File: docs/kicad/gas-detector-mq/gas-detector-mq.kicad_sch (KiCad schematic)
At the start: 8 parts, among them U1 ESP32_DevKit_V1, U2 MH-MQ-Sensor

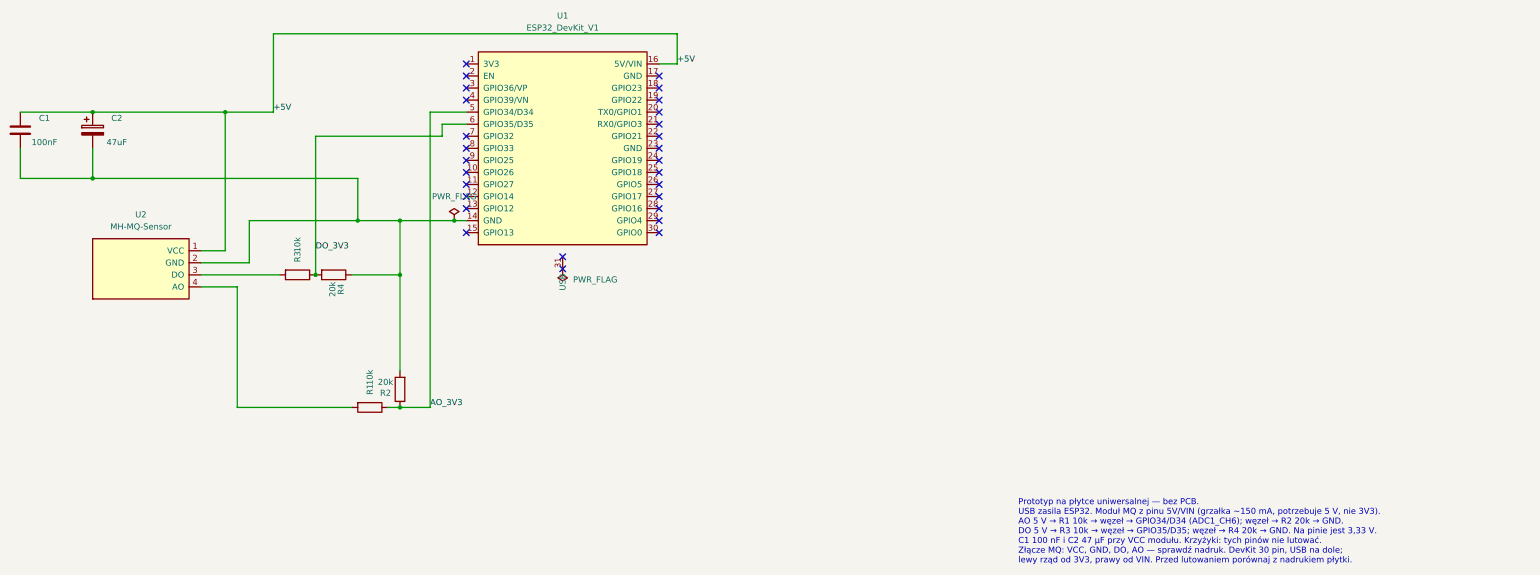
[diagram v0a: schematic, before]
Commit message: Zamień bulk 47 µF na 10 µF / 50 V.
Kondensator 100 nF zostaje. 1000 µF / 6,3 V nie wchodzi na szynę 5 V z USB: za mały zapas napięcia i duży udar przy wpięciu kabla.

Co-authored-by: michal.kalkowski <michal.kalkowski@sumup.com>
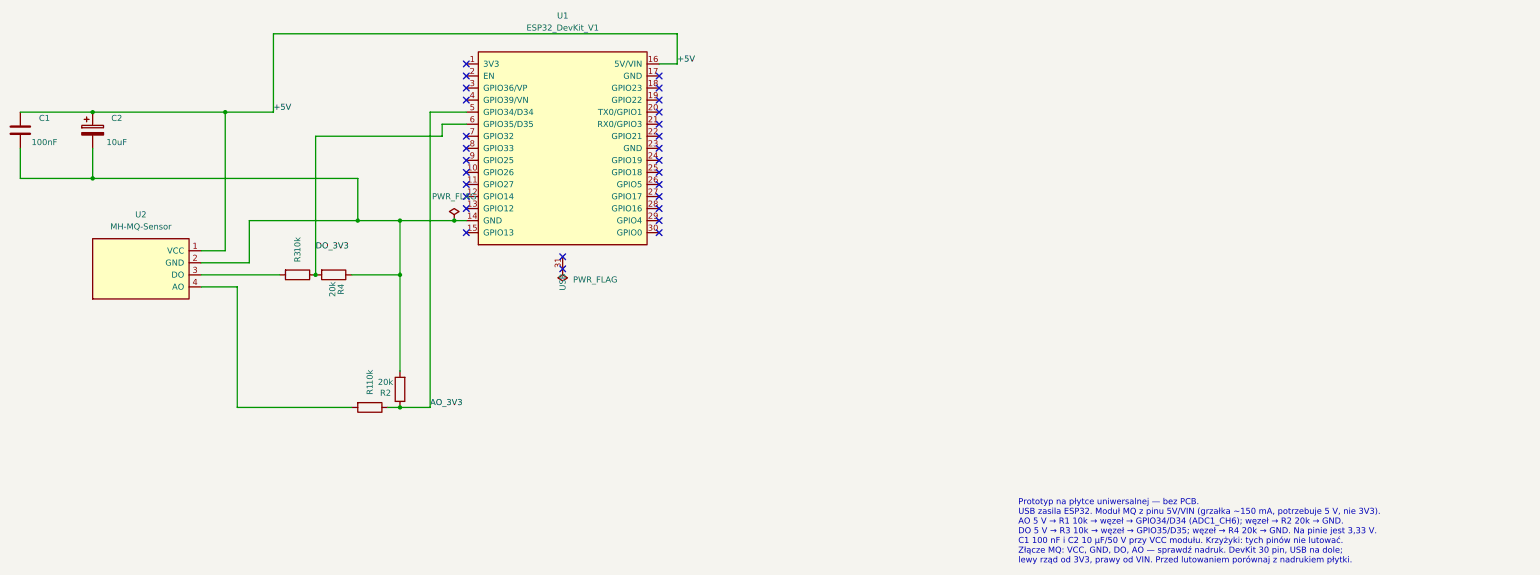
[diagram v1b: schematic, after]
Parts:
- C2: value 47uF -> 10uF
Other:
- note added: "Prototyp na płytce uniwersalnej — bez PCB. USB zasila ESP32. Moduł MQ z pinu 5V/VIN (grzałka ~150 mA, potrzebuje 5 V, nie 3V3). AO 5 V → R1 10k → węzeł → GPIO34/D34 (ADC1_CH6); węzeł → R2 20k → GND. DO 5 V → R3 10k → węzeł → GPIO35/D35; węzeł → R4 20k → GND. Na pinie jest 3,33 V. C1 100 nF i C2 10 µF/50 V przy VCC modułu. Krzyżyki: tych pinów nie lutować. Złącze MQ: VCC, GND, DO, AO — sprawdź nad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"
- note removed: "Prototyp na płytce uniwersalnej — bez PCB. USB zasila ESP32. Moduł MQ z pinu 5V/VIN (grzałka ~150 mA, potrzebuje 5 V, nie 3V3). AO 5 V → R1 10k → węzeł → GPIO34/D34 (ADC1_CH6); węzeł → R2 20k → GND. DO 5 V → R3 10k → węzeł → GPIO35/D35; węzeł → R4 20k → GND. Na pinie jest 3,33 V. C1 100 nF i C2 47 µF przy VCC modułu. Krzyżyki: tych pinów nie lutować. Złącze MQ: VCC, GND, DO, AO — sprawdź nadruk. 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"
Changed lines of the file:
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@@
 		(comment 3 "Założenie: DOIT DevKit V1 30 pin, USB na dole; złącze MQ VCC GND DO AO.")
 	)
-	(text "Prototyp na płytce uniwersalnej — bez PCB.\nUSB zasila ESP32. Moduł MQ z pinu 5V/VIN (grzałka ~150 mA, potrzebuje 5 V, nie 3V3).\nAO 5 V → R1 10k → węzeł → GPIO34/D34 (ADC1_CH6); węzeł → R2 20k → GND.\nDO 5 V → R3 10k → węzeł → GPIO35/D35; węzeł → R4 20k → GND. Na pinie jest 3,33 V.\nC1 100 nF i C2 47 µF przy VCC modułu. Krzyżyki: tych pinów nie lutować.\nZłącze MQ: VCC, GND, DO, AO — sprawdź nadruk. DevKit 30 pin, USB na dole;\nlewy rząd od 3V3, prawy od VIN. Przed lutowaniem porównaj z nadrukiem płytki."
+	(text "Prototyp na płytce uniwersalnej — bez PCB.\nUSB zasila ESP32. Moduł MQ z pinu 5V/VIN (grzałka ~150 mA, potrzebuje 5 V, nie 3V3).\nAO 5 V → R1 10k → węzeł → GPIO34/D34 (ADC1_CH6); węzeł → R2 20k → GND.\nDO 5 V → R3 10k → węzeł → GPIO35/D35; węzeł → R4 20k → GND. Na pinie jest 3,33 V.\nC1 100 nF i C2 10 µF/50 V przy VCC modułu. Krzyżyki: tych pinów nie lutować.\nZłącze MQ: VCC, GND, DO, AO — sprawdź nadruk. DevKit 30 pin, USB na dole;\nlewy rząd od 3V3, prawy od VIN. Przed lutowaniem porównaj z nadrukiem płytki."
 		(exclude_from_sim no)
 		(at 301.752 236.474 0)
@@
 			)
 		)
-		(property "Value" "47uF"
+		(property "Value" "10uF"
 			(at 111.76 161.29 0)
 			(show_name no)

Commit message: Wstaw na C2 elektrolit 47 µF / 50 V.
Ta wartość pasuje do zakupu THT Low ESR i do lokalnego bulk przy module MQ.

Co-authored-by: michal.kalkowski <michal.kalkowski@sumup.com>
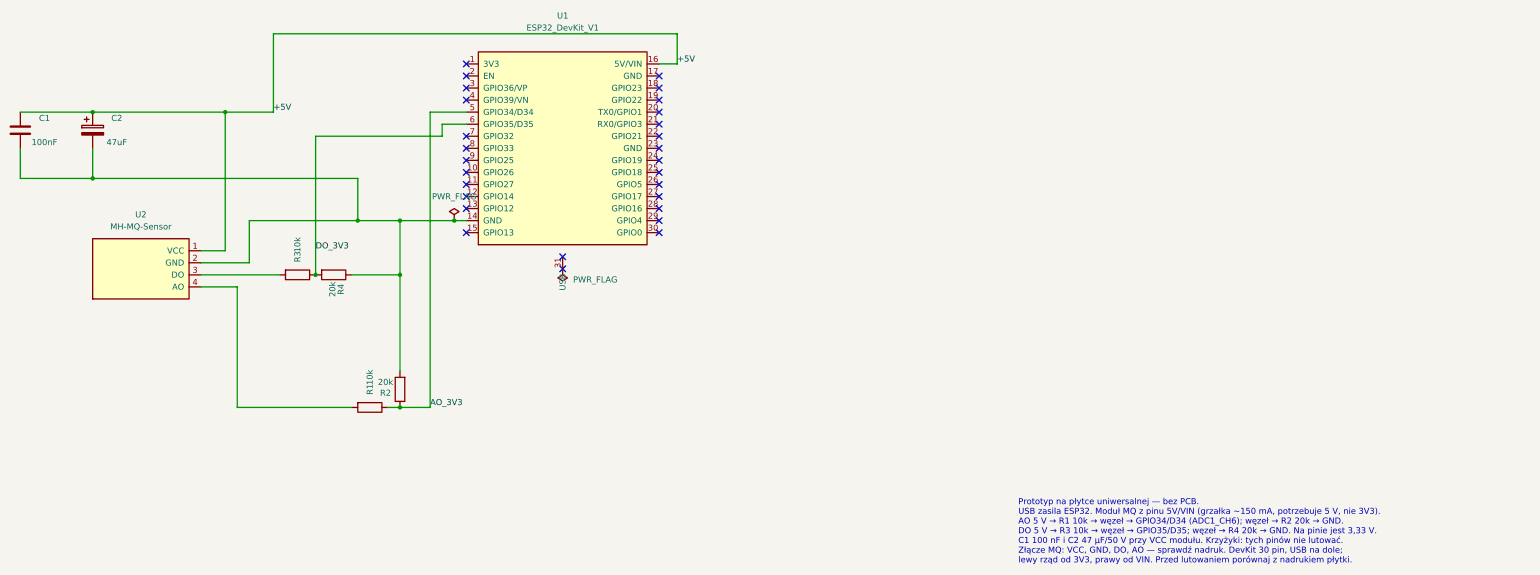
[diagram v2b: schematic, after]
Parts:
- C2: value 10uF -> 47uF
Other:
- note added: "Prototyp na płytce uniwersalnej — bez PCB. USB zasila ESP32. Moduł MQ z pinu 5V/VIN (grzałka ~150 mA, potrzebuje 5 V, nie 3V3). AO 5 V → R1 10k → węzeł → GPIO34/D34 (ADC1_CH6); węzeł → R2 20k → GND. DO 5 V → R3 10k → węzeł → GPIO35/D35; węzeł → R4 20k → GND. Na pinie jest 3,33 V. C1 100 nF i C2 47 µF/50 V przy VCC modułu. Krzyżyki: tych pinów nie lutować. Złącze MQ: VCC, GND, DO, AO — sprawdź nad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"
- note removed: "Prototyp na płytce uniwersalnej — bez PCB. USB zasila ESP32. Moduł MQ z pinu 5V/VIN (grzałka ~150 mA, potrzebuje 5 V, nie 3V3). AO 5 V → R1 10k → węzeł → GPIO34/D34 (ADC1_CH6); węzeł → R2 20k → GND. DO 5 V → R3 10k → węzeł → GPIO35/D35; węzeł → R4 20k → GND. Na pinie jest 3,33 V. C1 100 nF i C2 10 µF/50 V przy VCC modułu. Krzyżyki: tych pinów nie lutować. Złącze MQ: VCC, GND, DO, AO — sprawdź nad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"
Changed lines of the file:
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@@
 		(comment 3 "Założenie: DOIT DevKit V1 30 pin, USB na dole; złącze MQ VCC GND DO AO.")
 	)
-	(text "Prototyp na płytce uniwersalnej — bez PCB.\nUSB zasila ESP32. Moduł MQ z pinu 5V/VIN (grzałka ~150 mA, potrzebuje 5 V, nie 3V3).\nAO 5 V → R1 10k → węzeł → GPIO34/D34 (ADC1_CH6); węzeł → R2 20k → GND.\nDO 5 V → R3 10k → węzeł → GPIO35/D35; węzeł → R4 20k → GND. Na pinie jest 3,33 V.\nC1 100 nF i C2 10 µF/50 V przy VCC modułu. Krzyżyki: tych pinów nie lutować.\nZłącze MQ: VCC, GND, DO, AO — sprawdź nadruk. DevKit 30 pin, USB na dole;\nlewy rząd od 3V3, prawy od VIN. Przed lutowaniem porównaj z nadrukiem płytki."
+	(text "Prototyp na płytce uniwersalnej — bez PCB.\nUSB zasila ESP32. Moduł MQ z pinu 5V/VIN (grzałka ~150 mA, potrzebuje 5 V, nie 3V3).\nAO 5 V → R1 10k → węzeł → GPIO34/D34 (ADC1_CH6); węzeł → R2 20k → GND.\nDO 5 V → R3 10k → węzeł → GPIO35/D35; węzeł → R4 20k → GND. Na pinie jest 3,33 V.\nC1 100 nF i C2 47 µF/50 V przy VCC modułu. Krzyżyki: tych pinów nie lutować.\nZłącze MQ: VCC, GND, DO, AO — sprawdź nadruk. DevKit 30 pin, USB na dole;\nlewy rząd od 3V3, prawy od VIN. Przed lutowaniem porównaj z nadrukiem płytki."
 		(exclude_from_sim no)
 		(at 301.752 236.474 0)
@@
 			)
 		)
-		(property "Value" "10uF"
+		(property "Value" "47uF"
 			(at 111.76 161.29 0)
 			(show_name no)
